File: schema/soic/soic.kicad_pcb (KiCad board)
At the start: 2 copper layers, 33.7 x 13 mm, 7 parts, among them J1 Conn_01x04_Male, J2 Conn_01x04_Male, U1 LF398_SOIC8

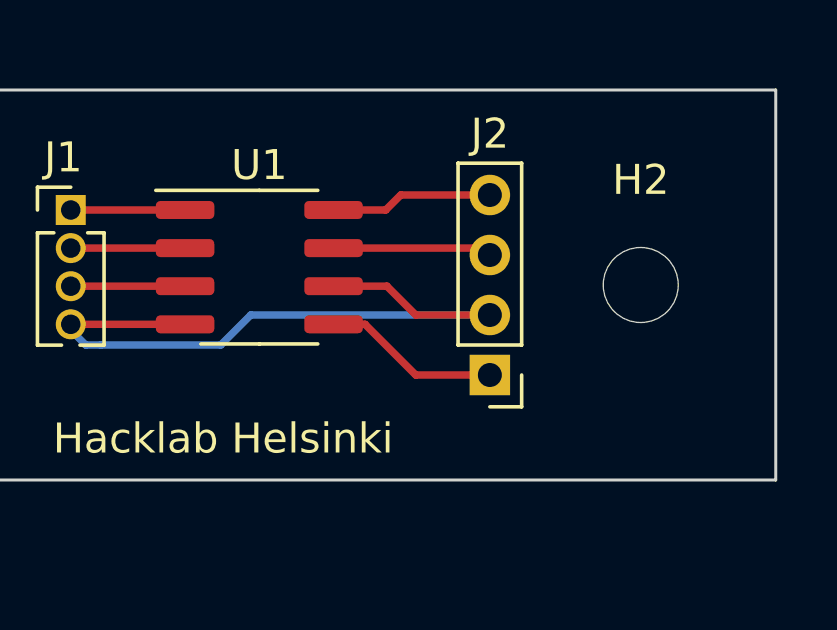
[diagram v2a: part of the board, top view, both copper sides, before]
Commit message: added via to example soic
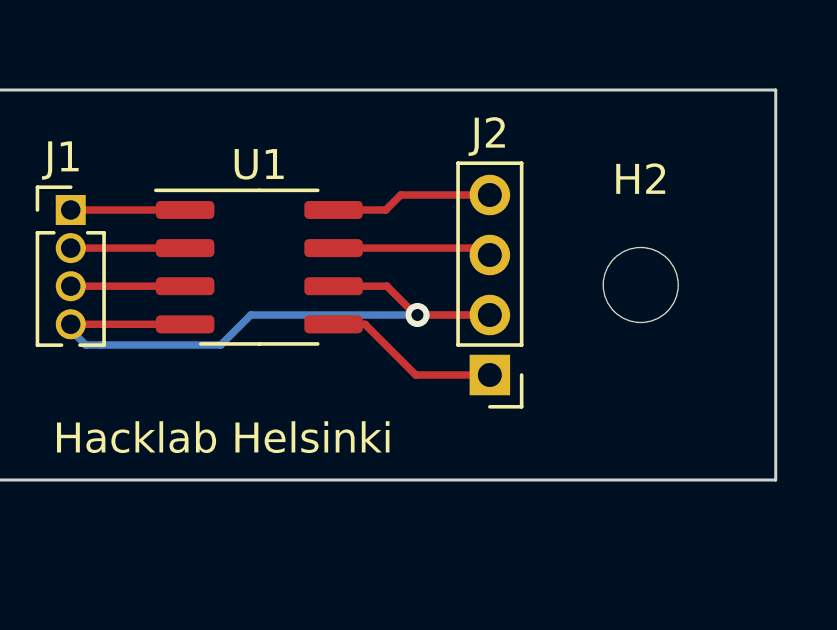
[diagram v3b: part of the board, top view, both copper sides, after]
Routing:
- net Net-(J1-Pad4): vias 0 -> 1
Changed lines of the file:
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@@
     (thickness 1.6)
     (drawings 5)
-    (tracks 19)
+    (tracks 21)
     (zones 0)
     (modules 7)
@@
       (effects (font (size 1 1) (thickness 0.15)))
     )
+    (fp_circle (center 0 0) (end 2.1 0) (layer Cmts.User) (width 0.15))
     (fp_circle (center 0 0) (end 2.35 0) (layer F.CrtYd) (width 0.05))
-    (fp_circle (center 0 0) (end 2.1 0) (layer Cmts.User) (width 0.15))
     (fp_text user %R (at 0.3 0) (layer F.Fab)
       (effects (font (size 1 1) (thickness 0.15)))
@@
       (effects (font (size 1 1) (thickness 0.15)))
     )
+    (fp_circle (center 0 0) (end 2.1 0) (layer Cmts.User) (width 0.15))
     (fp_circle (center 0 0) (end 2.35 0) (layer F.CrtYd) (width 0.05))
-    (fp_circle (center 0 0) (end 2.1 0) (layer Cmts.User) (width 0.15))
     (fp_text user %R (at 0.3 0) (layer F.Fab)
       (effects (font (size 1 1) (thickness 0.15)))
@@
       (effects (font (size 1 1) (thickness 0.15)))
     )
+    (fp_circle (center 0 0) (end 2.5 0) (layer Cmts.User) (width 0.15))
     (fp_circle (center 0 0) (end 2.75 0) (layer F.CrtYd) (width 0.05))
-    (fp_circle (center 0 0) (end 2.5 0) (layer Cmts.User) (width 0.15))
     (fp_text user %R (at 0.3 0) (layer F.Fab)
       (effects (font (size 1 1) (thickness 0.15)))
@@
       (effects (font (size 1 1) (thickness 0.15)))
     )
+    (fp_circle (center 0 0) (end 2.5 0) (layer Cmts.User) (width 0.15))
     (fp_circle (center 0 0) (end 2.75 0) (layer F.CrtYd) (width 0.05))
-    (fp_circle (center 0 0) (end 2.5 0) (layer Cmts.User) (width 0.15))
     (fp_text user %R (at 0.3 0) (layer F.Fab)
       (effects (font (size 1 1) (thickness 0.15)))
@@
       (effects (font (size 1 1) (thickness 0.15)))
     )
+    (fp_line (start 1.5 -1.5) (end -1.5 -1.5) (layer F.CrtYd) (width 0.05))
+    (fp_line (start 1.5 7.5) (end 1.5 -1.5) (layer F.CrtYd) (width 0.05))
+    (fp_line (start -1.5 7.5) (end 1.5 7.5) (layer F.CrtYd) (width 0.05))
+    (fp_line (start -1.5 -1.5) (end -1.5 7.5) (layer F.CrtYd) (width 0.05))
+    (fp_line (start -1.06 -1.06) (end 0 -1.06) (layer F.SilkS) (width 0.12))
+    (fp_line (start -1.06 0) (end -1.06 -1.06) (layer F.SilkS) (width 0.12))
+    (fp_line (start -1.06 1) (end 1.06 1) (layer F.SilkS) (width 0.12))
+    (fp_line (start 1.06 1) (end 1.06 7.06) (layer F.SilkS) (width 0.12))
+    (fp_line (start -1.06 1) (end -1.06 7.06) (layer F.SilkS) (width 0.12))
+    (fp_line (start -1.06 7.06) (end 1.06 7.06) (layer F.SilkS) (width 0.12))
+    (fp_line (start -1 -0.5) (end -0.5 -1) (layer F.Fab) (width 0.1))
+    (fp_line (start -1 7) (end -1 -0.5) (layer F.Fab) (width 0.1))
+    (fp_line (start 1 7) (end -1 7) (layer F.Fab) (width 0.1))
+    (fp_line (start 1 -1) (end 1 7) (layer F.Fab) (width 0.1))
     (fp_line (start -0.5 -1) (end 1 -1) (layer F.Fab) (width 0.1))
-    (fp_line (start 1 -1) (end 1 7) (layer F.Fab) (width 0.1))
-    (fp_line (start 1 7) (end -1 7) (layer F.Fab) (width 0.1))
-    (fp_line (start -1 7) (end -1 -0.5) (layer F.Fab) (width 0.1))
-    (fp_line (start -1 -0.5) (end -0.5 -1) (layer F.Fab) (width 0.1))
-    (fp_line (start -1.06 7.06) (end 1.06 7.06) (layer F.SilkS) (width 0.12))
-    (fp_line (start -1.06 1) (end -1.06 7.06) (layer F.SilkS) (width 0.12))
-    (fp_line (start 1.06 1) (end 1.06 7.06) (layer F.SilkS) (width 0.12))
-    (fp_line (start -1.06 1) (end 1.06 1) (layer F.SilkS) (width 0.12))
-    (fp_line (start -1.06 0) (end -1.06 -1.06) (layer F.SilkS) (width 0.12))
-    (fp_line (start -1.06 -1.06) (end 0 -1.06) (layer F.SilkS) (width 0.12))
-    (fp_line (start -1.5 -1.5) (end -1.5 7.5) (layer F.CrtYd) (width 0.05))
-    (fp_line (start -1.5 7.5) (end 1.5 7.5) (layer F.CrtYd) (width 0.05))
-    (fp_line (start 1.5 7.5) (end 1.5 -1.5) (layer F.CrtYd) (width 0.05))
-    (fp_line (start 1.5 -1.5) (end -1.5 -1.5) (layer F.CrtYd) (width 0.05))
     (fp_text user %R (at 0 3 90) (layer F.Fab)
       (effects (font (size 1 1) (thickness 0.15)))
@@
       (effects (font (size 1 1) (thickness 0.15)))
     )
+    (fp_line (start 1.55 -1.15) (end -1.55 -1.15) (layer F.CrtYd) (width 0.05))
+    (fp_line (start 1.55 4.95) (end 1.55 -1.15) (layer F.CrtYd) (width 0.05))
+    (fp_line (start -1.55 4.95) (end 1.55 4.95) (layer F.CrtYd) (width 0.05))
+    (fp_line (start -1.55 -1.15) (end -1.55 4.95) (layer F.CrtYd) (width 0.05))
+    (fp_line (start -1.11 -0.76) (end 0 -0.76) (layer F.SilkS) (width 0.12))
+    (fp_line (start -1.11 0) (end -1.11 -0.76) (layer F.SilkS) (width 0.12))
+    (fp_line (start 0.563471 0.76) (end 1.11 0.76) (layer F.SilkS) (width 0.12))
+    (fp_line (start -1.11 0.76) (end -0.563471 0.76) (layer F.SilkS) (width 0.12))
+    (fp_line (start 1.11 0.76) (end 1.11 4.505) (layer F.SilkS) (width 0.12))
+    (fp_line (start -1.11 0.76) (end -1.11 4.505) (layer F.SilkS) (width 0.12))
+    (fp_line (start 0.30753 4.505) (end 1.11 4.505) (layer F.SilkS) (width 0.12))
+    (fp_line (start -1.11 4.505) (end -0.30753 4.505) (layer F.SilkS) (width 0.12))
+    (fp_line (start -1.05 -0.11) (end -0.525 -0.635) (layer F.Fab) (width 0.1))
+    (fp_line (start -1.05 4.445) (end -1.05 -0.11) (layer F.Fab) (width 0.1))
+    (fp_line (start 1.05 4.445) (end -1.05 4.445) (layer F.Fab) (width 0.1))
+    (fp_line (start 1.05 -0.635) (end 1.05 4.445) (layer F.Fab) (width 0.1))
     (fp_line (start -0.525 -0.635) (end 1.05 -0.635) (layer F.Fab) (width 0.1))
-    (fp_line (start 1.05 -0.635) (end 1.05 4.445) (layer F.Fab) (width 0.1))
-    (fp_line (start 1.05 4.445) (end -1.05 4.445) (layer F.Fab) (width 0.1))
-    (fp_line (start -1.05 4.445) (end -1.05 -0.11) (layer F.Fab) (width 0.1))
-    (fp_line (start -1.05 -0.11) (end -0.525 -0.635) (layer F.Fab) (width 0.1))
-    (fp_line (start -1.11 4.505) (end -0.30753 4.505) (layer F.SilkS) (width 0.12))
-    (fp_line (start 0.30753 4.505) (end 1.11 4.505) (layer F.SilkS) (width 0.12))
-    (fp_line (start -1.11 0.76) (end -1.11 4.505) (layer F.SilkS) (width 0.12))
-    (fp_line (start 1.11 0.76) (end 1.11 4.505) (layer F.SilkS) (width 0.12))
-    (fp_line (start -1.11 0.76) (end -0.563471 0.76) (layer F.SilkS) (width 0.12))
-    (fp_line (start 0.563471 0.76) (end 1.11 0.76) (layer F.SilkS) (width 0.12))
-    (fp_line (start -1.11 0) (end -1.11 -0.76) (layer F.SilkS) (width 0.12))
-    (fp_line (start -1.11 -0.76) (end 0 -0.76) (layer F.SilkS) (width 0.12))
-    (fp_line (start -1.55 -1.15) (end -1.55 4.95) (layer F.CrtYd) (width 0.05))
-    (fp_line (start -1.55 4.95) (end 1.55 4.95) (layer F.CrtYd) (width 0.05))
-    (fp_line (start 1.55 4.95) (end 1.55 -1.15) (layer F.CrtYd) (width 0.05))
-    (fp_line (start 1.55 -1.15) (end -1.55 -1.15) (layer F.CrtYd) (width 0.05))
     (fp_text user %R (at 0 1.905 90) (layer F.Fab)
       (effects (font (size 1 1) (thickness 0.15)))
@@
       (effects (font (size 1 1) (thickness 0.15)))
     )
+    (fp_line (start 3.7 -2.7) (end -3.7 -2.7) (layer F.CrtYd) (width 0.05))
+    (fp_line (start 3.7 2.7) (end 3.7 -2.7) (layer F.CrtYd) (width 0.05))
+    (fp_line (start -3.7 2.7) (end 3.7 2.7) (layer F.CrtYd) (width 0.05))
+    (fp_line (start -3.7 -2.7) (end -3.7 2.7) (layer F.CrtYd) (width 0.05))
+    (fp_line (start -1.95 -1.475) (end -0.975 -2.45) (layer F.Fab) (width 0.1))
+    (fp_line (start -1.95 2.45) (end -1.95 -1.475) (layer F.Fab) (width 0.1))
+    (fp_line (start 1.95 2.45) (end -1.95 2.45) (layer F.Fab) (width 0.1))
+    (fp_line (start 1.95 -2.45) (end 1.95 2.45) (layer F.Fab) (width 0.1))
+    (fp_line (start -0.975 -2.45) (end 1.95 -2.45) (layer F.Fab) (width 0.1))
+    (fp_line (start 0 -2.56) (end -3.45 -2.56) (layer F.SilkS) (width 0.12))
+    (fp_line (start 0 -2.56) (end 1.95 -2.56) (layer F.SilkS) (width 0.12))
+    (fp_line (start 0 2.56) (end -1.95 2.56) (layer F.SilkS) (width 0.12))
     (fp_line (start 0 2.56) (end 1.95 2.56) (layer F.SilkS) (width 0.12))
-    (fp_line (start 0 2.56) (end -1.95 2.56) (layer F.SilkS) (width 0.12))
-    (fp_line (start 0 -2.56) (end 1.95 -2.56) (layer F.SilkS) (width 0.12))
-    (fp_line (start 0 -2.56) (end -3.45 -2.56) (layer F.SilkS) (width 0.12))
-    (fp_line (start -0.975 -2.45) (end 1.95 -2.45) (layer F.Fab) (width 0.1))
-    (fp_line (start 1.95 -2.45) (end 1.95 2.45) (layer F.Fab) (width 0.1))
-    (fp_line (start 1.95 2.45) (end -1.95 2.45) (layer F.Fab) (width 0.1))
-    (fp_line (start -1.95 2.45) (end -1.95 -1.475) (layer F.Fab) (width 0.1))
-    (fp_line (start -1.95 -1.475) (end -0.975 -2.45) (layer F.Fab) (width 0.1))
-    (fp_line (start -3.7 -2.7) (end -3.7 2.7) (layer F.CrtYd) (width 0.05))
-    (fp_line (start -3.7 2.7) (end 3.7 2.7) (layer F.CrtYd) (width 0.05))
-    (fp_line (start 3.7 2.7) (end 3.7 -2.7) (layer F.CrtYd) (width 0.05))
-    (fp_line (start 3.7 -2.7) (end -3.7 -2.7) (layer F.CrtYd) (width 0.05))
     (fp_text user %R (at 0 0) (layer F.Fab)
       (effects (font (size 0.98 0.98) (thickness 0.15)))
@@
   (segment (start 18.89 -11.4028) (end 20.67 -11.4028) (width 0.25) (layer F.Cu) (net 1))
   (segment (start 20.67 -11.4028) (end 21.63 -10.4428) (width 0.25) (layer F.Cu) (net 1))
-  (segment (start 21.63 -10.4428) (end 24.13 -10.4428) (width 0.25) (layer F.Cu) (net 1))
+  (segment (start 21.63 -10.4428) (end 21.688 -10.4428) (width 0.25) (layer F.Cu) (net 1))
   (segment (start 24.1 -10.4428) (end 16.13 -10.4428) (width 0.25) (layer B.Cu) (net 1))
   (segment (start 16.13 -10.4428) (end 15.13 -9.4428) (width 0.25) (layer B.Cu) (net 1))
@@
   (segment (start 11.13 -9.4428) (end 10.63 -9.4428) (width 0.25) (layer B.Cu) (net 1))
   (segment (start 10.63 -9.4428) (end 10.13 -9.9428) (width 0.25) (layer B.Cu) (net 1))
+  (segment (start 21.688 -10.4428) (end 24.13 -10.4428) (width 0.25) (layer F.Cu) (net 1))
+  (via (at 21.688 -10.4428) (size 0.8) (drill 0.4) (layers F.Cu B.Cu) (net 1))
   (segment (start 10.13 -11.4028) (end 13.94 -11.4028) (width 0.25) (layer F.Cu) (net 2))
   (segment (start 10.13 -12.6728) (end 13.94 -12.6728) (width 0.25) (layer F.Cu) (net 3))

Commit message: ardrill command, pad2pad&soic projects
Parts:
- removed H3, H4: MountingHole, MountingHole:MountingHole_2.1mm
- moved H1 18.0 mm to (-11.9, -5.44)
- moved H2 18.0 mm to (12.1, -5.44)
- moved J1 18.0 mm to (-6.87, -7.94)
- moved J2 18.0 mm to (7.10, -2.44)
- moved U1 18.0 mm to (-0.58, -6.04)
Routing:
- net (no net): vias 0 -> 2
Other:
- board size 33.7 x 13 mm -> 30 x 11 mm

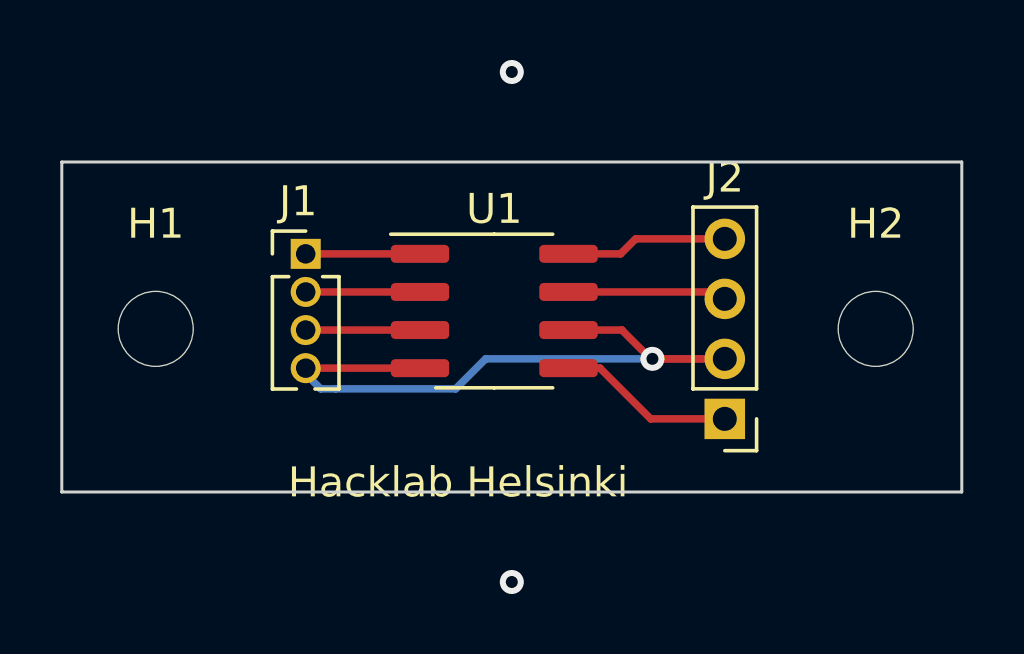
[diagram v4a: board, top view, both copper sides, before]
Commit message: support 02-silk directory
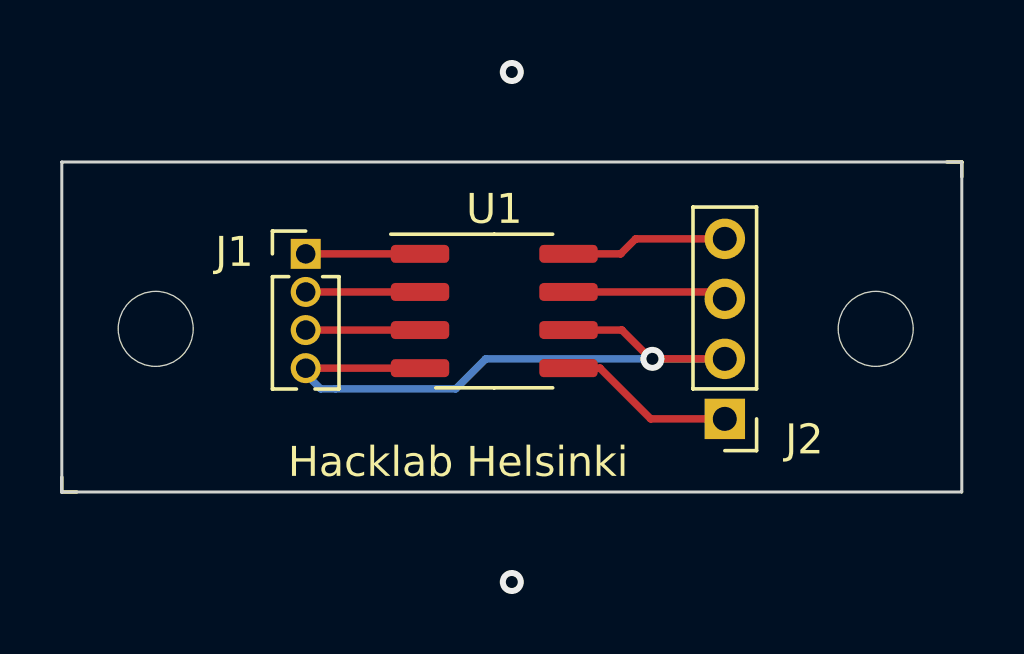
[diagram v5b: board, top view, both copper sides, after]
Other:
- board text added: "bot left"
- board text added: "bot right"
- board text added: "soic-B 26.6.2022/jj"
- board text added: "top left"
- board text added: "top right"

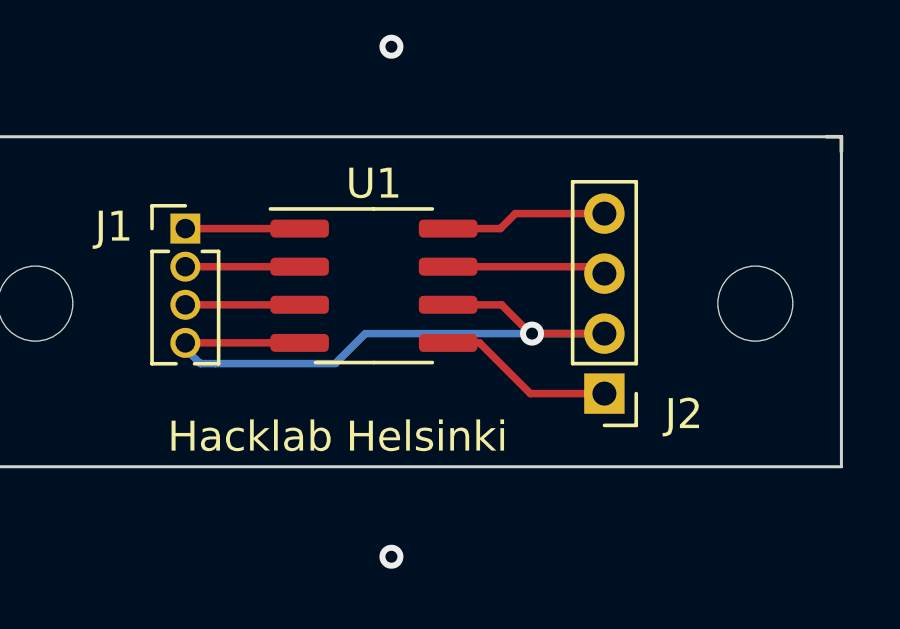
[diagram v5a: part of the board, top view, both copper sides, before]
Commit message: soic example: added 0603 pad, added track between soic pads
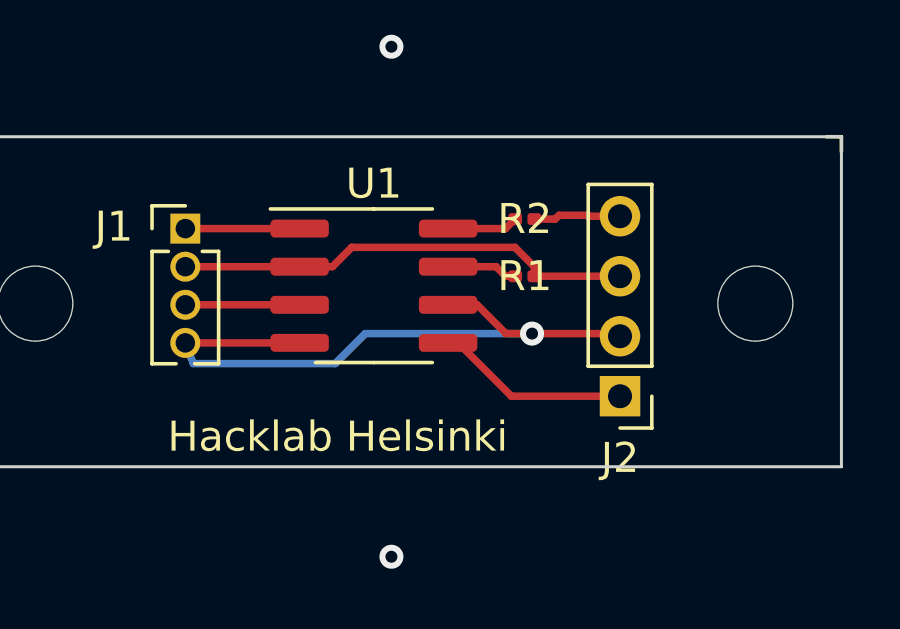
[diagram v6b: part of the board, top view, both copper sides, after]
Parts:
- added R1: 0, Resistor_SMD:R_0201_0603Metric, F.Cu at (4.45, -6.35)
- added R2: 0, Resistor_SMD:R_0201_0603Metric, F.Cu at (4.45, -8.26)
- moved J2 0.53 mm to (7.62, -2.35)
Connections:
- J2 pad 3: Net-(J2-Pad3) -> Net-(J1-Pad2)
- U1 pad 7: Net-(J2-Pad3) -> Net-(R1-Pad1)
- U1 pad 8: Net-(J2-Pad4) -> Net-(R2-Pad1)
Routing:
- net Net-(J1-Pad2): track 3.81 -> 15.3 mm
- net Net-(J2-Pad3): track 5.01 -> 0.00 mm
- net Net-(J2-Pad4): track 5.45 -> 2.92 mm
- net Net-(R1-Pad1): track 0.00 -> 2.37 mm
- net Net-(R2-Pad1): track 0.00 -> 2.37 mm
- net Net-(J1-Pad4): track 24.0 -> 21.7 mm
- net Net-(J2-Pad1): track 5.94 -> 6.47 mm
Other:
- net class Default removed
